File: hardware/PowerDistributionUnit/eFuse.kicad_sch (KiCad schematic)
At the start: 25 parts, among them Q2 CSD18511Q5A, U4 AD5258, U5 TPS25983

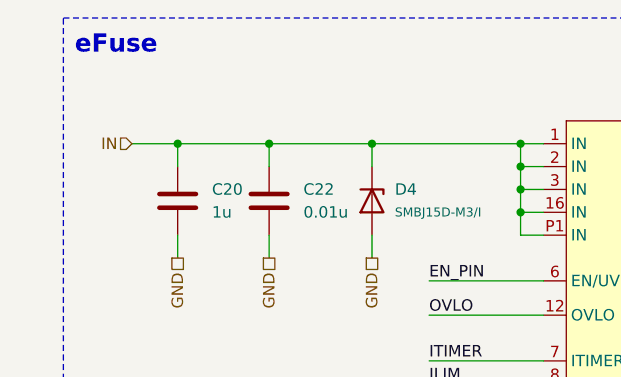
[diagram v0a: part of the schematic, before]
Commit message: fixed Lakshay review things (CAN DC-DC output caps, DC-DC symbol name update, fix CAN eFuse isolation, add CAN connectors, DC-DC RC jumper, voltage label) and removed PG int from EN mux
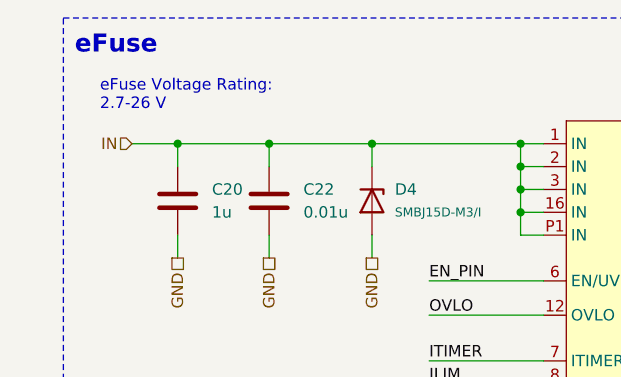
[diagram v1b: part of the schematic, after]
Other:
- note added: "eFuse Voltage Rating: 2.7-26 V"
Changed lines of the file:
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@@
+		)
+	)
+	(text "eFuse Voltage Rating:\n2.7-26 V"
+		(exclude_from_sim no)
+		(at 21.844 28.956 0)
+		(effects
+			(font
+				(size 1.27 1.27)
+			)
+			(justify left)
 		)
 	)

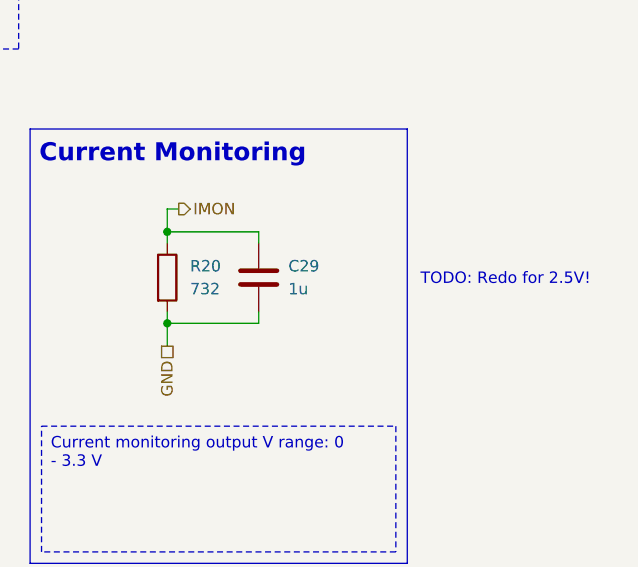
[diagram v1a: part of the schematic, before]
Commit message: Continued revising eFuse isolation. Also fixed pulls on ADCMUX
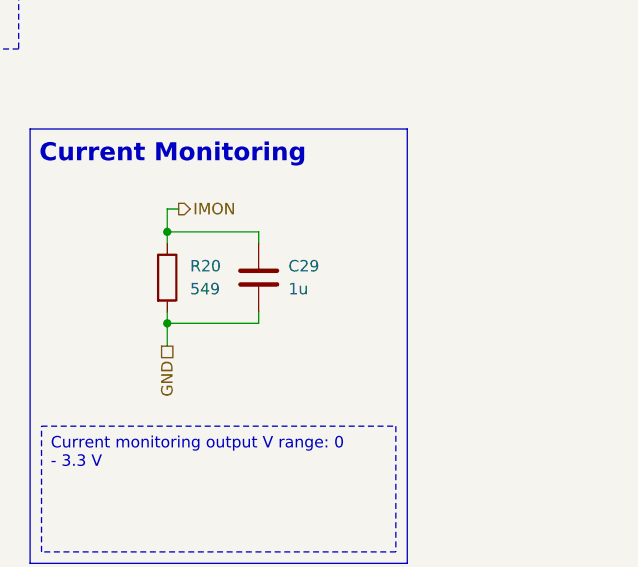
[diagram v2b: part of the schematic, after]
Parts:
- R20: value 732 -> 549
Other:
- note removed: "TODO: Redo for 2.5V!"
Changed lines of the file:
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@@
 		)
 	)
-	(text "TODO: Redo for 2.5V!"
-		(exclude_from_sim no)
-		(at 259.842 117.094 0)
-		(effects
-			(font
-				(size 1.27 1.27)
-				(color 255 0 0 1)
-			)
-		)
-	)
 	(text "UVLO functionality of eFuse\nnot used to be able to use \nEN as an ON/OFF control. "
 		(exclude_from_sim no)
@@
 			)
 		)
-		(property "Value" "732"
+		(property "Value" "549"
 			(at 224.79 118.1099 0)
 			(effects

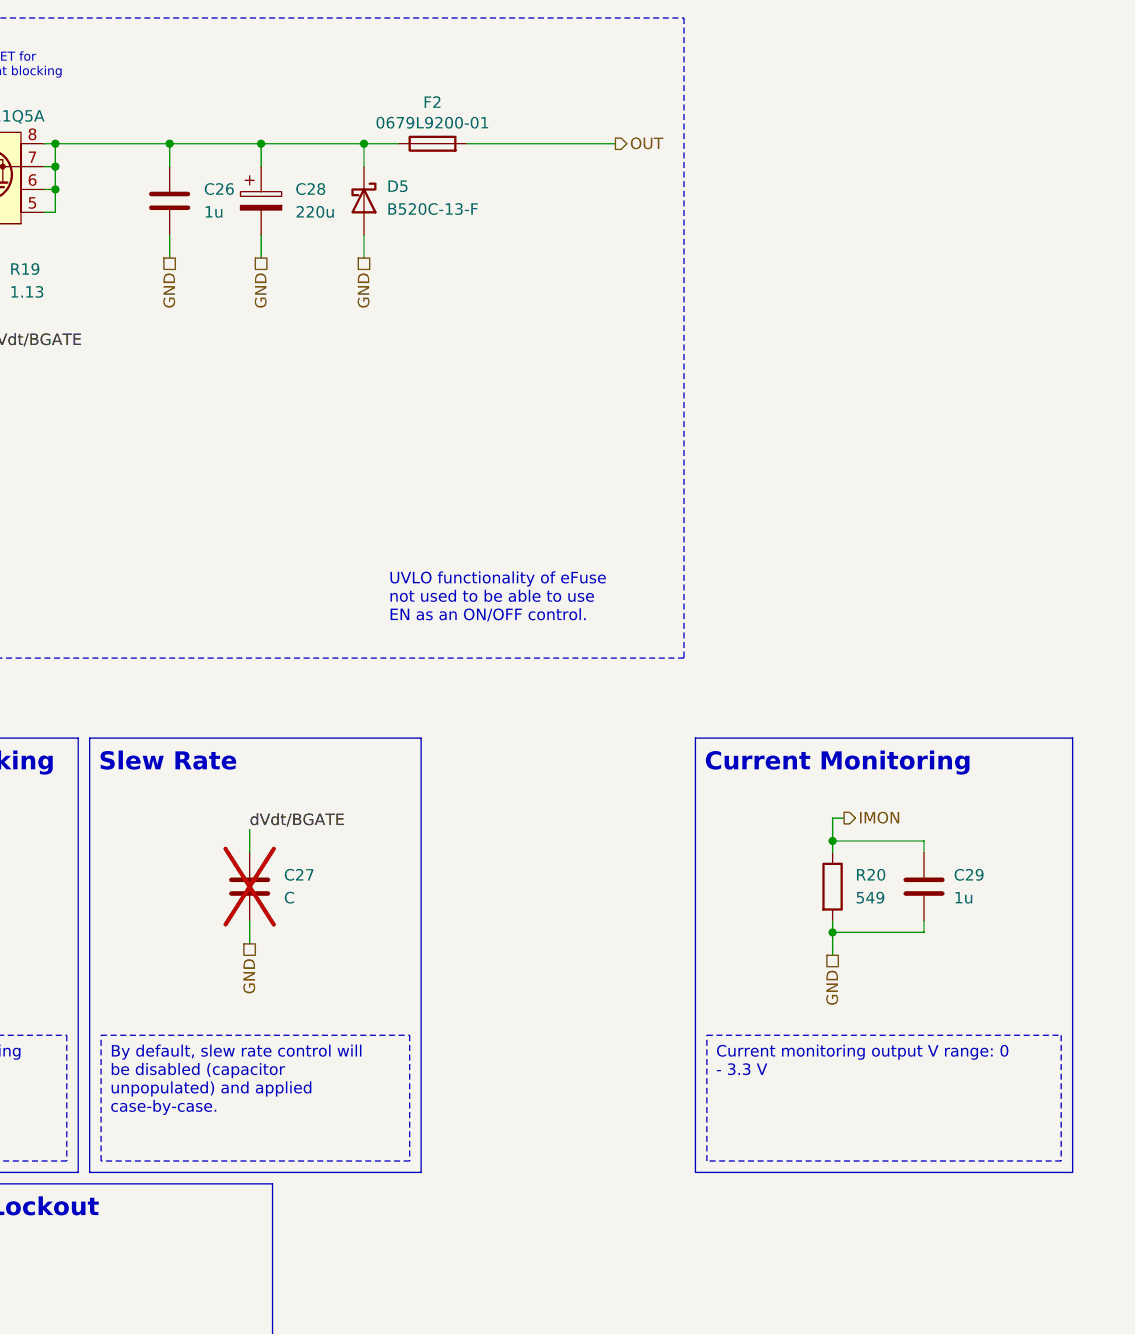
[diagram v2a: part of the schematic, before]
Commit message: Added footprints, added pull-up resistors, finished wiring up SOM
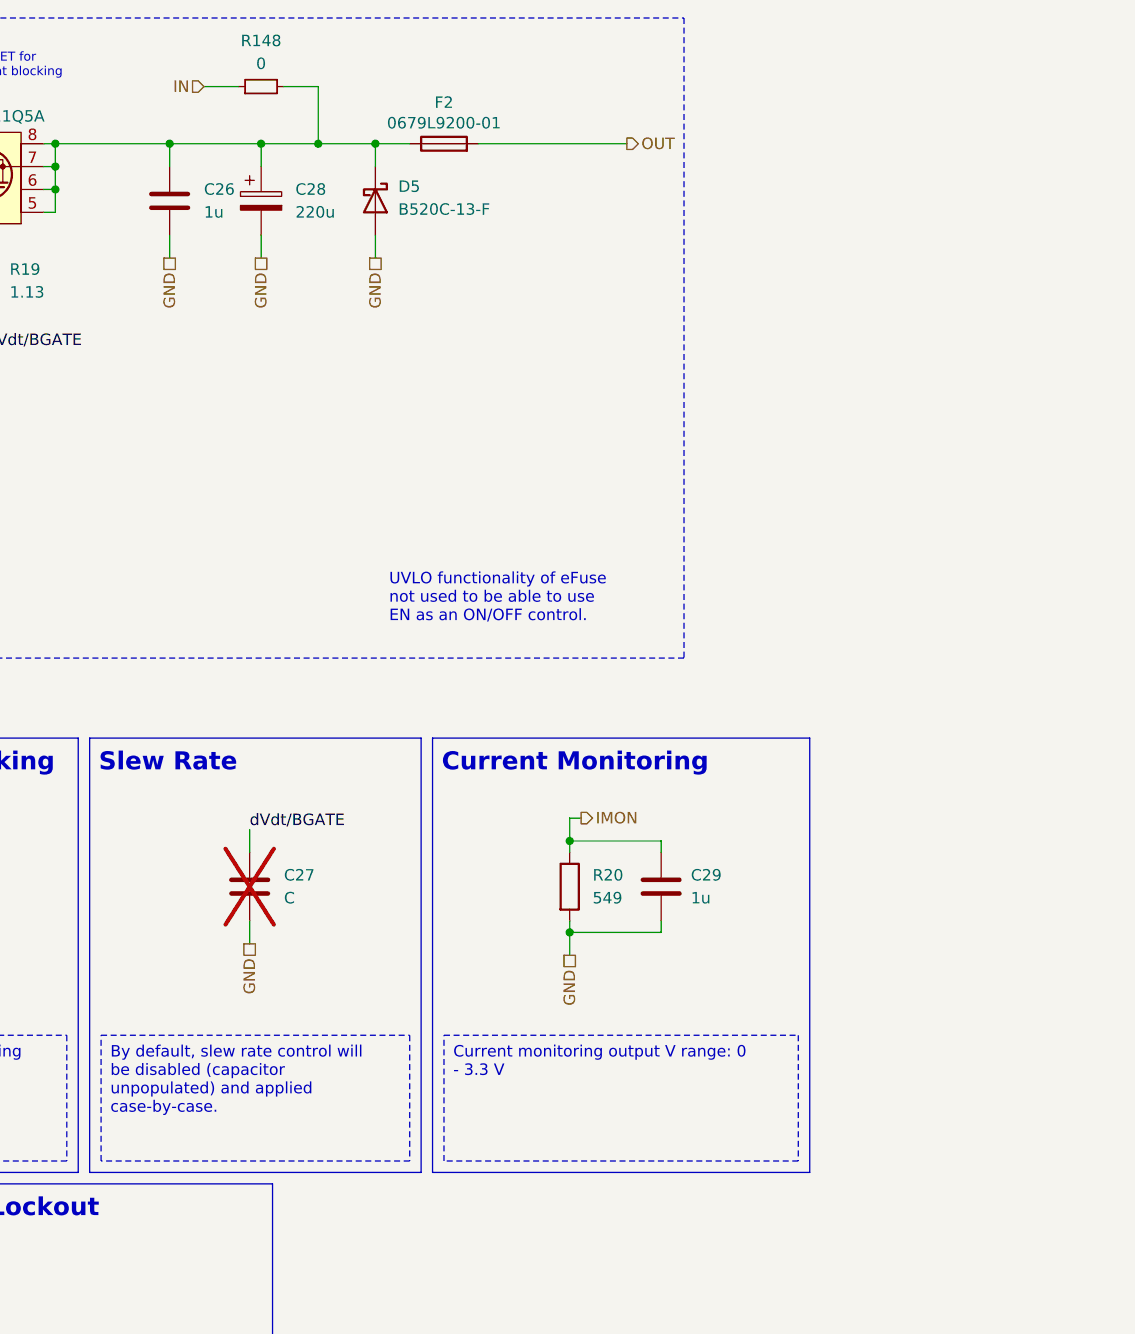
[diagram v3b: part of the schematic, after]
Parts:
- added R148: 0, symbol Device:R_Small
- C28: footprint (none) -> Capacitor_SMD:CP_Elec_10x10.5
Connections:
- net IN: now also R148.1
- net at C26.1, C28.1, D5.1 (K)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: now also R148.2
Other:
- moved on the sheet: C29, D5, F2, R20

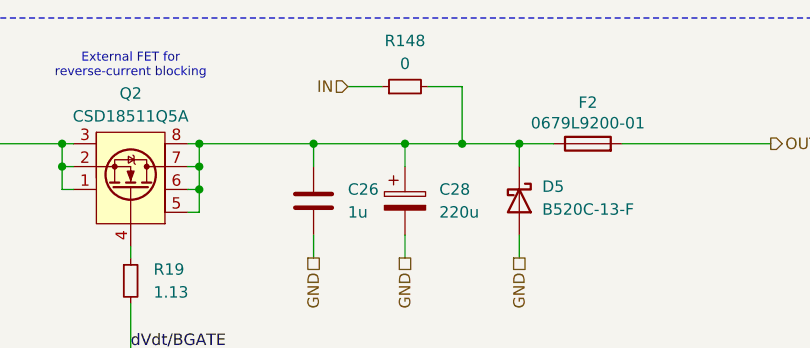
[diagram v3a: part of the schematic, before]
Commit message: Added non populated 0 ohm resistor
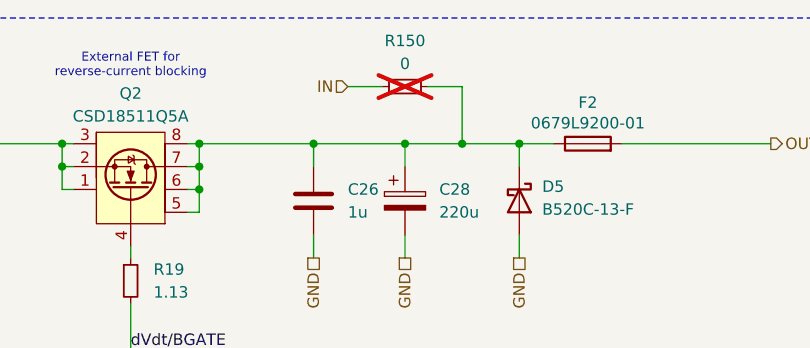
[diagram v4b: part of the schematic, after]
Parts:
- R150: renamed from R148; now not fitted
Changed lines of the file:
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@@
 		(in_bom yes)
 		(on_board yes)
-		(dnp no)
+		(dnp yes)
 		(fields_autoplaced yes)
-		(property "Reference" "R148"
+		(property "Reference" "R150"
 			(at 158.75 22.86 90)
 			(effects

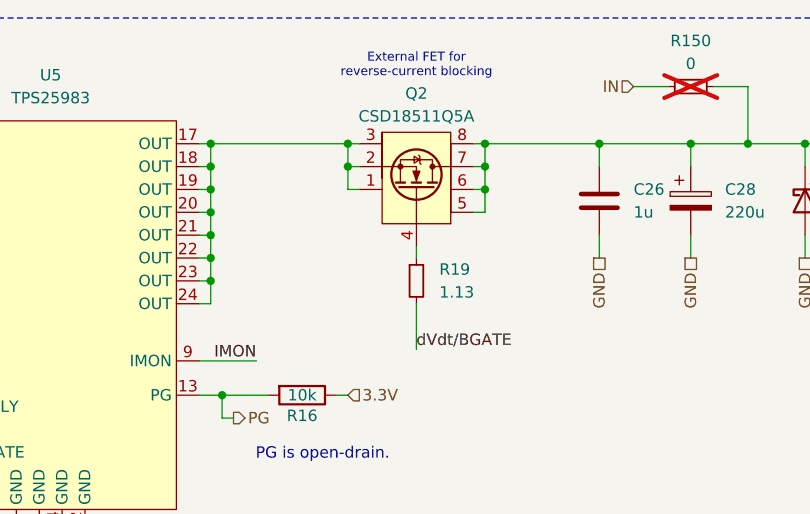
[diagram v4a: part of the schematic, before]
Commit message: fixed tps25983 footprint pads, reverse current blocking mosfet symbol, and removed auto_saved_files
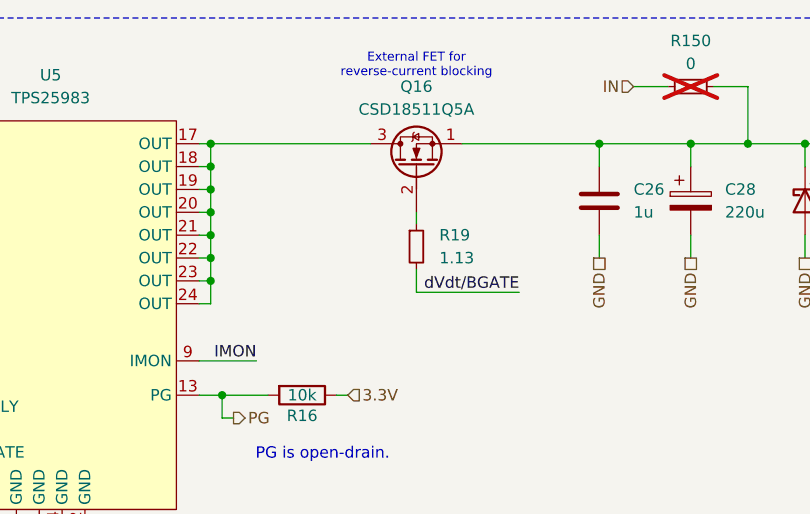
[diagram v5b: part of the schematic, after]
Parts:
- removed Q2: CSD18511Q5A, Package_SON:VSONP-8-1EP_5x6_P1.27mm, symbol PowerDistributionUnitLib:CSD18511Q5A
- added Q16: CSD18511Q5A, Package_SON:VSONP-8-1EP_5x6_P1.27mm, symbol Device:Q_NMOS_SGD
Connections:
- net at R19.1: now also Q16.2 (G)
- net at C26.1, C28.1, D5.1 (K)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: now also Q16.1 (S)
- net at U5.17 (OUT), U5.18 (OUT), U5.19 (OUT)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: now also Q16.3 (D)
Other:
- moved on the sheet: R19

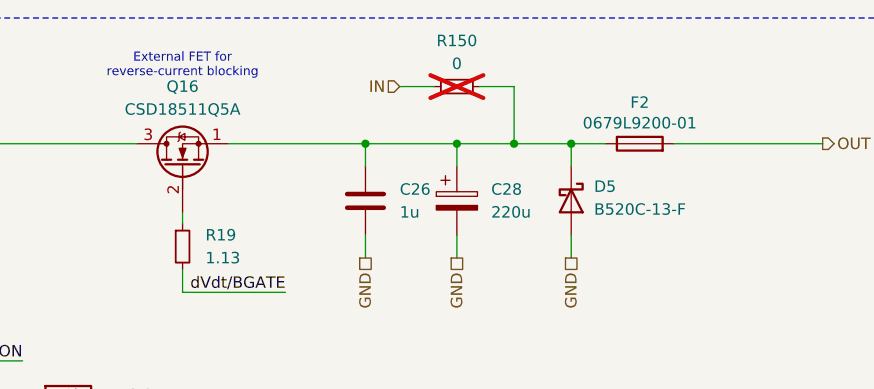
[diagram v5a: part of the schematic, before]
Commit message: changed fuse
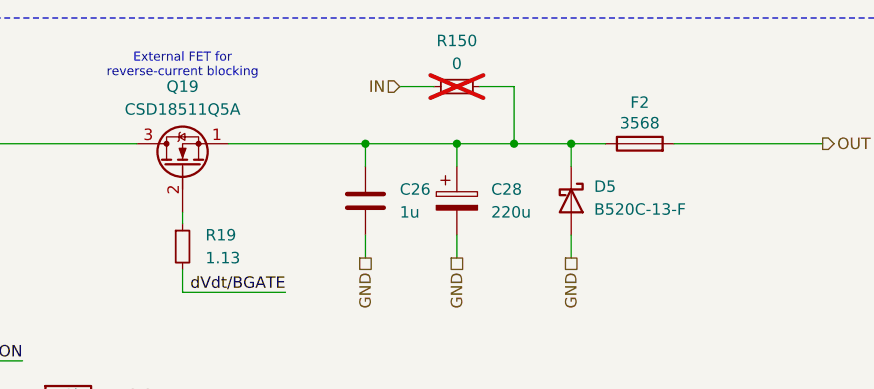
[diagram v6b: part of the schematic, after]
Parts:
- F2: value 0679L9200-01 -> 3568; footprint (none) -> Fuse:Fuseholder_Blade_Mini_Keystone_3568
- renumbered Q16 to Q19
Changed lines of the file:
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@@
 			)
 		)
-		(property "Value" "0679L9200-01"
+		(property "Value" "3568"
 			(at 179.07 32.004 90)
 			(effects
@@
 			)
 		)
-		(property "Footprint" ""
+		(property "Footprint" "Fuse:Fuseholder_Blade_Mini_Keystone_3568"
 			(at 179.07 36.068 90)
 			(effects
@@
 		(dnp no)
 		(fields_autoplaced yes)
-		(property "Reference" "Q16"
+		(property "Reference" "Q19"
 			(at 128.27 27.94 90)
 			(effects
